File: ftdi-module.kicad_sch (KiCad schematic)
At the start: 58 parts, among them U1 AP62301_TSOT, U2 FT4232H_VQFN, U3 AP62301_TSOT, Y1 Resonator_12MHz_ABM8G

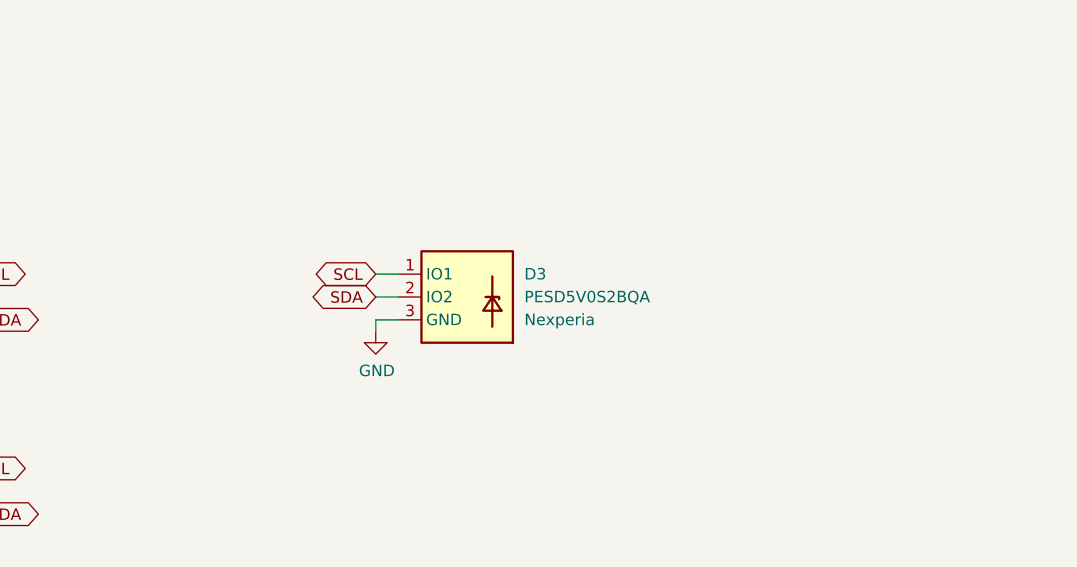
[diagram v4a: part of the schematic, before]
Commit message: Add fan arbiters for all outputs
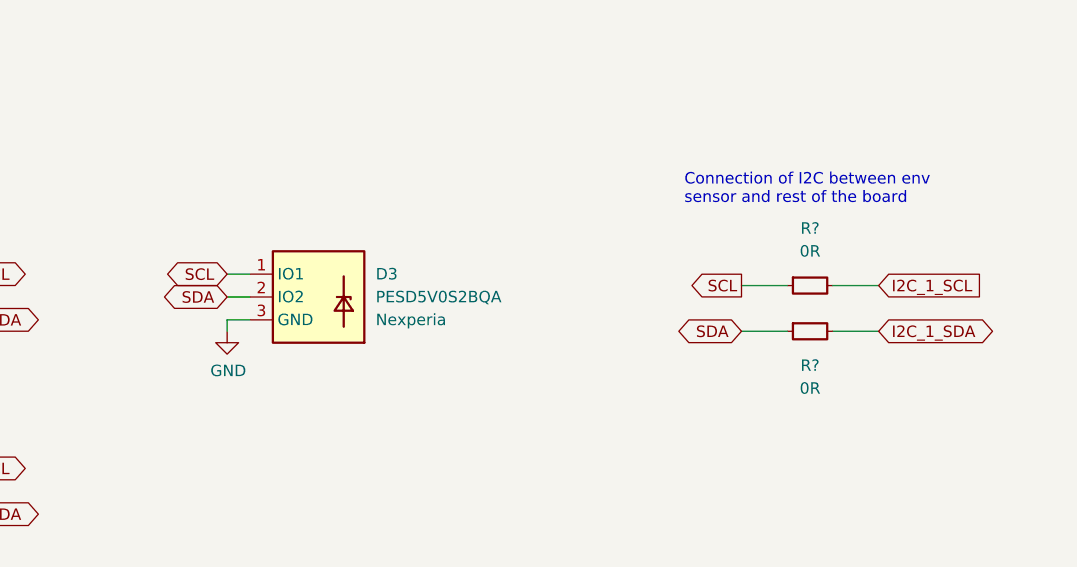
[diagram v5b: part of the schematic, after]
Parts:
- added R? (x2): R_0R_0402, antmicro-footprints:R_0402_1005Metric, symbol antmicroResistors0402:R_0R_0402
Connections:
- net SCL: now also R?.1
- net SDA: now also R?.1
- new net I2C_1_SCL: R?.2
- new net I2C_1_SDA: R?.2
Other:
- note added: "Connection of I2C between env sensor and rest of the board"
- moved on the sheet: D3

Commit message: Reannotate
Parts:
- gave numbers to parts that had none: 2
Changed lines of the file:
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@@
   (symbol (lib_id "antmicroResistors0402:R_0R_0402") (at 298.45 59.69 0) (unit 1)
     (in_bom yes) (on_board yes) (fields_autoplaced)
-    (property "Reference" "R?" (id 0) (at 300.99 63.5 0)
+    (property "Reference" "R18" (id 0) (at 300.99 63.5 0)
       (effects (font (size 1.27 1.27) (thickness 0.15)))
     )
@@
   (symbol (lib_id "antmicroResistors0402:R_0R_0402") (at 298.45 54.61 0) (unit 1)
     (in_bom yes) (on_board yes) (fields_autoplaced)
-    (property "Reference" "R?" (id 0) (at 300.99 48.26 0)
-      (effects (font (size 1.27 1.27) (thickness 0.15)))
-    )
+    (property "Reference" "R17" (id 0) (at 300.99 48.26 0)
+      (effects (font (size 1.27 1.27) (thickness 0.15)))
+    )

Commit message: Additional cleanup
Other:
- note removed: "replace with LDO"
- title: D1600E PSU Breakout Board -> GPU Cluster Backplane
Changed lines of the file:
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@@
   (paper "A3")
   (title_block
-    (title "D1600E PSU Breakout Board")
+    (title "GPU Cluster Backplane")
     (date "2023-10-18")
     (rev "1.0.0")
@@
     )
   )
-  (text "replace with LDO\n" (at 95.25 185.42 0)
-    (effects (font (size 1.27 1.27)) (justify left bottom))
-  )
   (text "3V3 DC/DC Converter" (at 213.36 189.865 0)

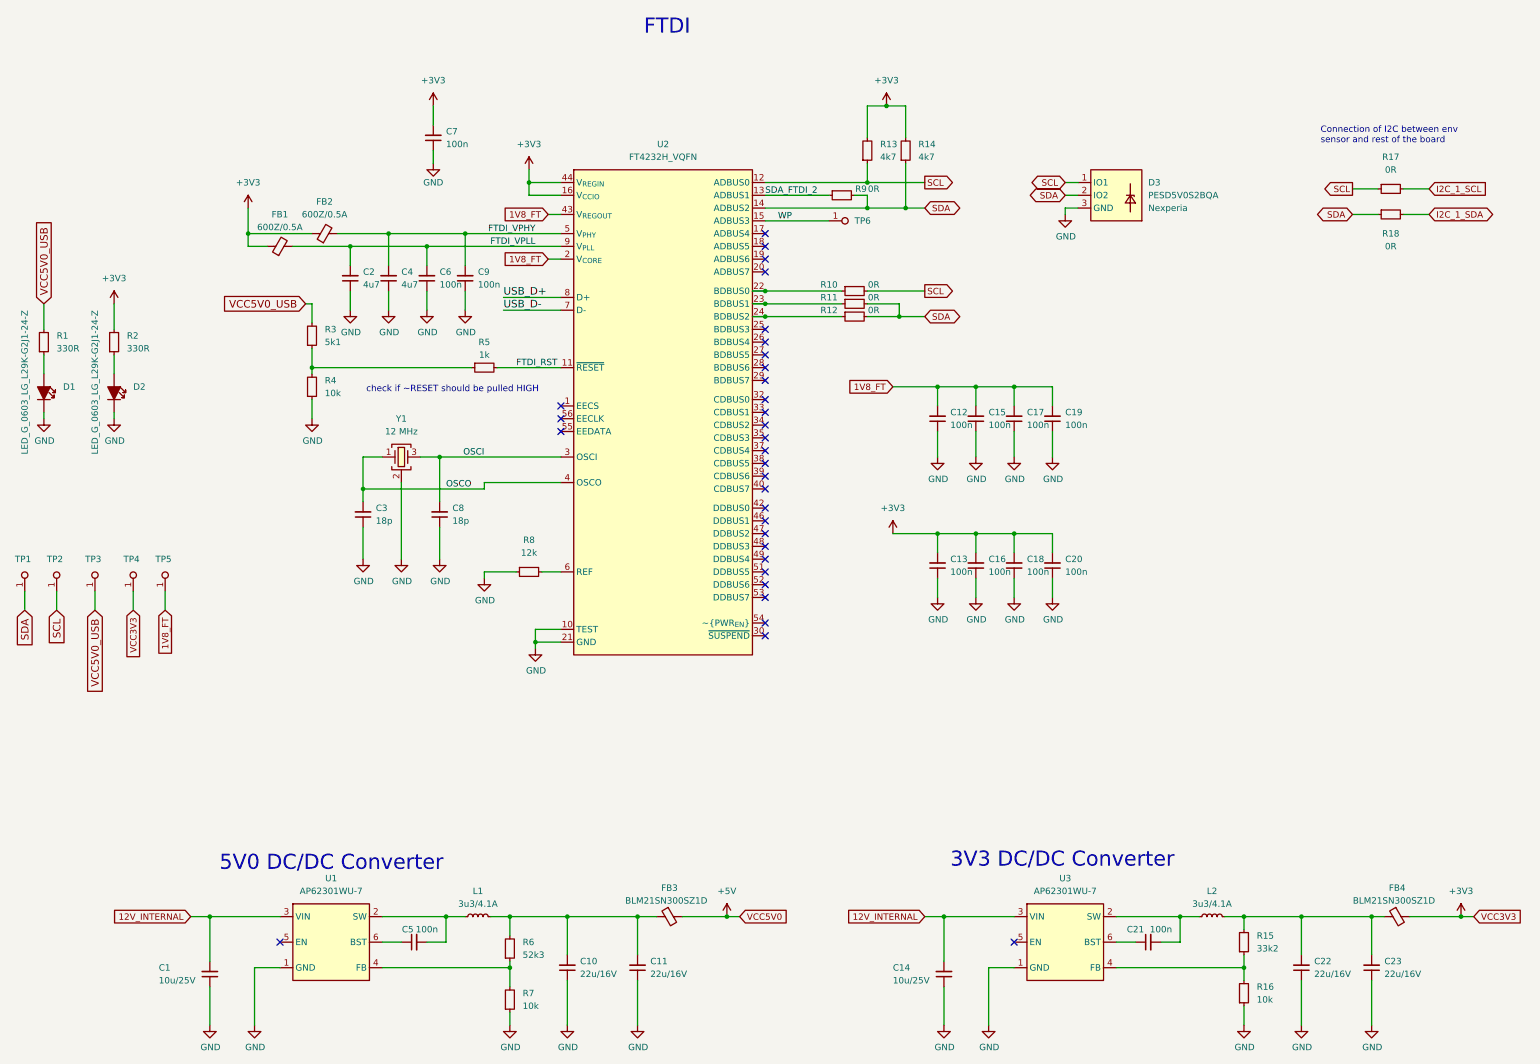
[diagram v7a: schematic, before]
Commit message: Minor fixes in schematic layout and reannotate
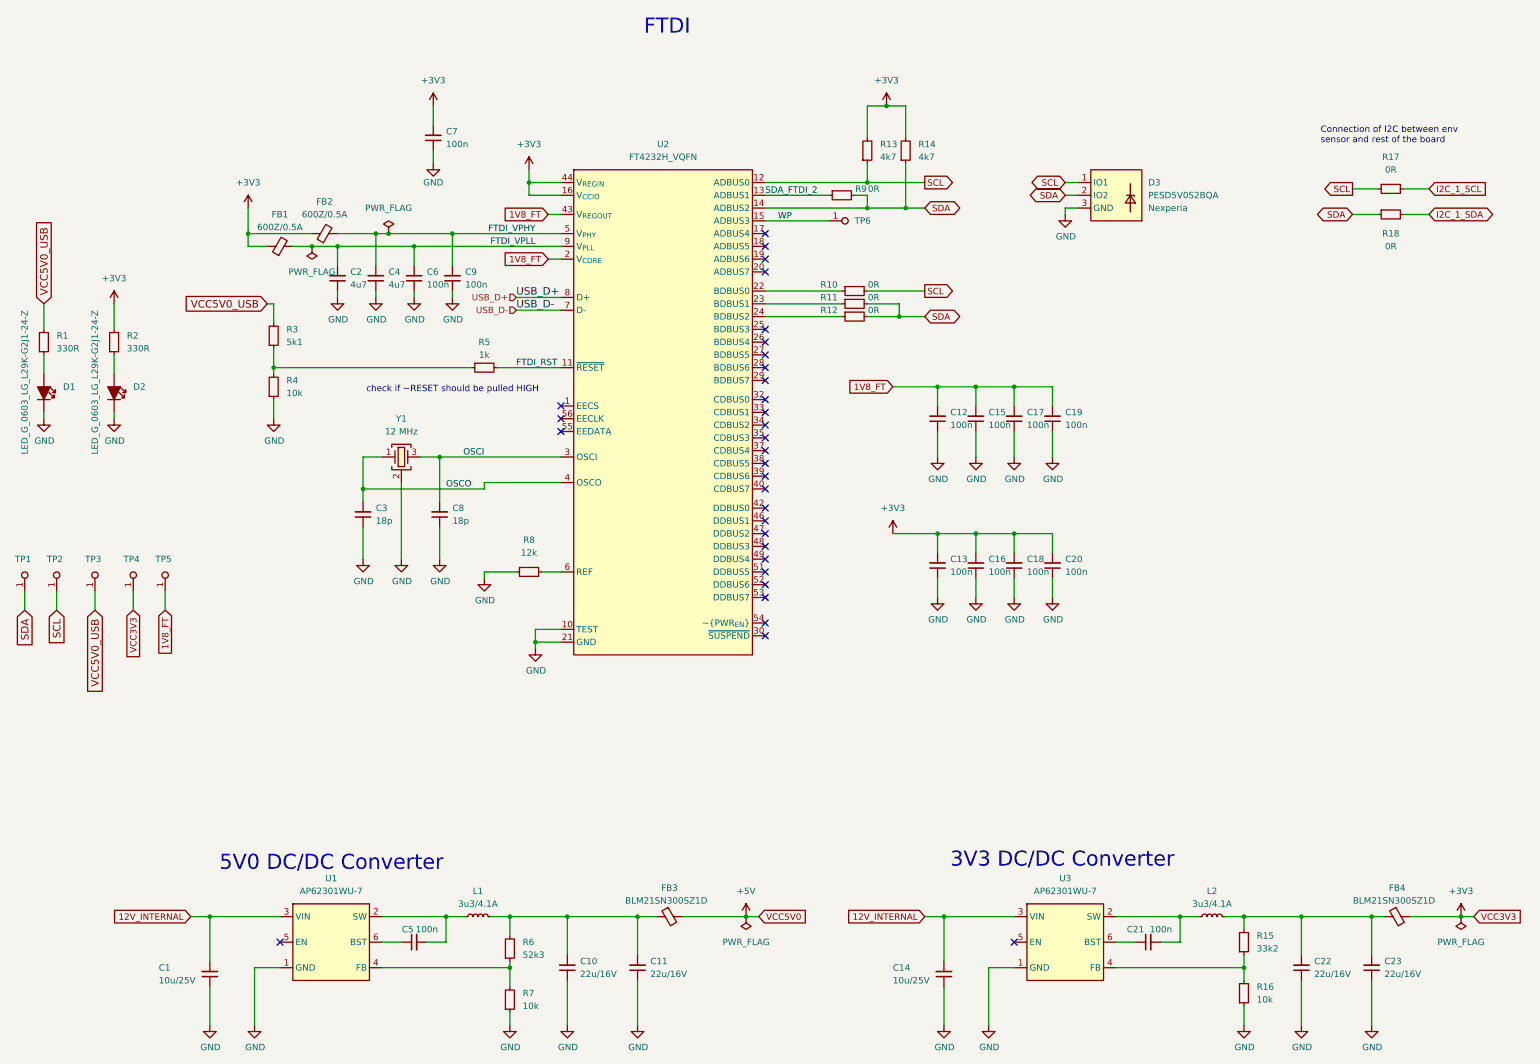
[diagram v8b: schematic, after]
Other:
- moved on the sheet: C2, C4, C6, C9, R3, R4
